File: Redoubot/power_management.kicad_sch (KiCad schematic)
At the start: 22 parts, among them U4 BQ25896RTWR, U5 BQ27220YZFR

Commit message: feat: added all remaining connectors & finished putting values on components
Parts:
- removed R19: 10m, Package_SON:Texas_S-PDSO-N12, symbol Device:R
- added C4: 1µF, symbol Device:C_Small
- added C5: 2.2µF, symbol Device:C_Small
- added C6: 470nF, symbol Device:C_Small
- added R2: 10k, Package_DFN_QFN:QFN-56-1EP_7x7mm_P0.4mm_EP5.6x5.6mm, symbol Device:R_Small_US
- added R3: 10m, Resistor_THT:R_Array_SIP4, symbol Device:R_Small_US
- added R4: 10k, symbol Device:R_Small_US
- R15, R16: value R -> 2.2k
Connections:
- net BAT: now also U5.C1 (SRP), U5.C3 (BAT), C4.1, R3.2
- net GND: now also U5.B2 (VSS), C4.2, C5.2, C6.2, R4.1
- net SCL_BAT: now also U5.A3 (SCL)
- net SDA_BAT: now also U5.A2 (SDA)
- net BAT_CHG: now reaches C15.2, C17.2, U4.13 (BAT), U4.14 (BAT)
- net BAT_CHG: now also U5.C2 (SRN), R3.1
- net GPOUT_FUEL_GAUGE: now reaches U5.A1 (GPOUT)
- net GPOUT_FUEL_GAUGE: now also R2.2
- net at U5.B1 (VIN): now also R4.2
- net at U5.B3 (VDD): now also C5.1, C6.1
- new net +3.3V: R2.1
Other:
- note added: "Fuel Gauge"
- moved on the sheet: U5

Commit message: chore: wired everything possible atm, wrote down every missing links, waiting for .ioc to continue
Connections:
- net 3.3V is gone; now on net +3.3V: R11.1, R13.1, R14.1
- net 5V renamed +5V
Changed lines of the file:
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@@
 	(wire
 		(pts
-			(xy 152.4 63.5) (xy 165.1 63.5)
+			(xy 157.48 63.5) (xy 165.1 63.5)
 		)
 		(stroke
@@
 	(wire
 		(pts
-			(xy 162.56 43.18) (xy 161.29 43.18)
+			(xy 162.56 43.18) (xy 157.48 43.18)
 		)
 		(stroke
@@
 	(wire
 		(pts
-			(xy 152.4 60.96) (xy 165.1 60.96)
+			(xy 157.48 60.96) (xy 165.1 60.96)
 		)
 		(stroke
@@
 	(wire
 		(pts
-			(xy 222.25 71.12) (xy 227.33 71.12)
+			(xy 222.25 71.12) (xy 240.03 71.12)
 		)
 		(stroke
@@
 	(wire
 		(pts
-			(xy 152.4 55.88) (xy 162.56 55.88)
+			(xy 157.48 55.88) (xy 162.56 55.88)
 		)
 		(stroke
@@
 			)
 			(justify right bottom)
-		)
-	)
-	(global_label "+3.3V"
-		(shape input)
-		(at 161.29 43.18 180)
-		(fields_autoplaced yes)
-		(effects
-			(font
-				(size 1.27 1.27)
-			)
-			(justify right)
-		)
-		(property "Intersheetrefs" "${INTERSHEET_REFS}"
-			(at 152.62 43.18 0)
-			(hide yes)
-			(show_name no)
-			(do_not_autoplace no)
-			(effects
-				(font
-					(size 1.27 1.27)
-				)
-				(justify right)
-			)
 		)
 	)
@@
 	(hierarchical_label "GPOUT_FUEL_GAUGE"
 		(shape output)
-		(at 152.4 55.88 180)
+		(at 157.48 55.88 180)
 		(effects
 			(font
@@
 		)
 	)
-	(hierarchical_label "5V"
+	(hierarchical_label "+5V"
 		(shape input)
 		(at 52.07 27.94 0)
@@
 		)
 	)
+	(hierarchical_label "+3.3V"
+		(shape input)
+		(at 157.48 43.18 180)
+		(effects
+			(font
+				(size 1.27 1.27)
+			)
+			(justify right)
+		)
+	)
 	(hierarchical_label "BAT"
 		(shape input)
-		(at 227.33 71.12 0)
+		(at 240.03 71.12 0)
 		(effects
 			(font
@@
 	(hierarchical_label "SDA_BAT"
 		(shape bidirectional)
-		(at 152.4 60.96 180)
+		(at 157.48 60.96 180)
 		(effects
 			(font
@@
 		)
 	)
-	(hierarchical_label "3.3V"
+	(hierarchical_label "+3.3V"
 		(shape input)
 		(at 31.75 102.87 180)
@@
 	(hierarchical_label "SCL_BAT"
 		(shape input)
-		(at 152.4 63.5 180)
-		(effects
-			(font
+		(at 157.48 63.5 180)
+		(effects
+			(font

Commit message: simply added the JLCPCB Part # as an LCSC field in the component descriptions
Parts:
- U4: footprint RTW0024H -> footprints_BQ25:RTW0024H; LCSC (none) -> C181475
- U5: footprint YZF9_TEX -> footprints_BQ27:YZF9_TEX; LCSC (none) -> C528617
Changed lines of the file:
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@@
 			)
 		)
-		(property "Footprint" "RTW0024H"
+		(property "Footprint" "footprints_BQ25:RTW0024H"
 			(at 78.74 62.23 0)
 			(hide yes)
@@
 		)
 		(property "Description" ""
+			(at 78.74 62.23 0)
+			(hide yes)
+			(show_name no)
+			(do_not_autoplace no)
+			(effects
+				(font
+					(size 1.27 1.27)
+				)
+			)
+		)
+		(property "LCSC" "C181475"
 			(at 78.74 62.23 0)
 			(hide yes)
@@
 			)
 		)
-		(property "Footprint" "YZF9_TEX"
+		(property "Footprint" "footprints_BQ27:YZF9_TEX"
 			(at 165.1 58.42 0)
 			(hide yes)
@@
 			(at 165.1 58.42 0)
 			(hide yes)
+			(show_name no)
+			(do_not_autoplace no)
+			(effects
+				(font
+					(size 1.27 1.27)
+				)
+			)
+		)
+		(property "LCSC" "C528617"
+			(at 165.1 58.42 0)
+			(hide yes)

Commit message: Added footprints for capacitors
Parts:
- C11, C13, C14: footprint (none) -> Capacitor_SMD:C_0603_1608Metric
- C12, C15, C16, C17, C18: footprint (none) -> Capacitor_SMD:C_0805_2012Metric
- C4, C5, C6: footprint (none) -> Capacitor_SMD:C_0402_1005Metric
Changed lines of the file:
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@@
 			)
 		)
-		(property "Footprint" ""
+		(property "Footprint" "Capacitor_SMD:C_0805_2012Metric"
 			(at 58.42 38.4048 0)
 			(hide yes)
@@
 			)
 		)
-		(property "Footprint" ""
+		(property "Footprint" "Capacitor_SMD:C_0805_2012Metric"
 			(at 132.3848 31.75 0)
 			(hide yes)
@@
 			)
 		)
-		(property "Footprint" ""
+		(property "Footprint" "Capacitor_SMD:C_0402_1005Metric"
 			(at 234.95 59.69 0)
 			(hide yes)
@@
 			)
 		)
-		(property "Footprint" ""
+		(property "Footprint" "Capacitor_SMD:C_0805_2012Metric"
 			(at 123.4948 66.04 0)
 			(hide yes)
@@
 			)
 		)
-		(property "Footprint" ""
+		(property "Footprint" "Capacitor_SMD:C_0402_1005Metric"
 			(at 154.94 76.2 0)
 			(hide yes)
@@
 			)
 		)
-		(property "Footprint" ""
+		(property "Footprint" "Capacitor_SMD:C_0603_1608Metric"
 			(at 41.91 30.7848 0)
 			(hide yes)
@@
 			)
 		)
-		(property "Footprint" ""
+		(property "Footprint" "Capacitor_SMD:C_0603_1608Metric"
 			(at 101.9048 31.75 0)
 			(hide yes)
@@
 			)
 		)
-		(property "Footprint" ""
+		(property "Footprint" "Capacitor_SMD:C_0402_1005Metric"
 			(at 162.56 76.2 0)
 			(hide yes)
@@
 			)
 		)
-		(property "Footprint" ""
+		(property "Footprint" "Capacitor_SMD:C_0805_2012Metric"
 			(at 113.3348 66.04 0)
 			(hide yes)
@@
 			)
 		)
-		(property "Footprint" ""
+		(property "Footprint" "Capacitor_SMD:C_0603_1608Metric"
 			(at 108.2548 44.45 0)
 			(hide yes)
@@
 			)
 		)
-		(property "Footprint" ""
+		(property "Footprint" "Capacitor_SMD:C_0805_2012Metric"
 			(at 122.2248 31.75 0)
 			(hide yes)

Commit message: Added the footprints for the resistors, inductors and the crystal
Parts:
- D3, D4: footprint (none) -> LED_SMD:LED_0603_1608Metric
- L2: footprint (none) -> Inductor_SMD:L_Coilcraft_XxL4020
- R11, R12, R13, R14, R15, R16, R17, R18, R4: footprint (none) -> Resistor_SMD:R_0603_1608Metric
- R2: footprint Package_DFN_QFN:QFN-56-1EP_7x7mm_P0.4mm_EP5.6x5.6mm -> Resistor_SMD:R_0603_1608Metric
- R3: footprint Resistor_THT:R_Array_SIP4 -> Resistor_SMD:R_0805_2012Metric
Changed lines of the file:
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@@
 			)
 		)
-		(property "Footprint" ""
+		(property "Footprint" "LED_SMD:LED_0603_1608Metric"
 			(at 46.99 59.69 0)
 			(hide yes)
@@
 			)
 		)
-		(property "Footprint" ""
+		(property "Footprint" "LED_SMD:LED_0603_1608Metric"
 			(at 46.99 66.04 0)
 			(hide yes)
@@
 			)
 		)
-		(property "Footprint" ""
+		(property "Footprint" "Resistor_SMD:R_0603_1608Metric"
 			(at 54.61 67.818 90)
 			(hide yes)
@@
 			)
 		)
-		(property "Footprint" ""
+		(property "Footprint" "Resistor_SMD:R_0603_1608Metric"
 			(at 39.878 87.63 90)
 			(hide yes)
@@
 			)
 		)
-		(property "Footprint" ""
+		(property "Footprint" "Resistor_SMD:R_0603_1608Metric"
 			(at 210.82 59.69 0)
 			(hide yes)
@@
 			)
 		)
-		(property "Footprint" "Package_DFN_QFN:QFN-56-1EP_7x7mm_P0.4mm_EP5.6x5.6mm"
+		(property "Footprint" "Resistor_SMD:R_0603_1608Metric"
 			(at 162.56 50.8 0)
 			(hide yes)
@@
 			)
 		)
-		(property "Footprint" ""
+		(property "Footprint" "Resistor_SMD:R_0603_1608Metric"
 			(at 46.228 87.63 90)
 			(hide yes)
@@
 			)
 		)
-		(property "Footprint" ""
+		(property "Footprint" "Inductor_SMD:L_Coilcraft_XxL4020"
 			(at 113.03 31.75 0)
 			(hide yes)
@@
 			)
 		)
-		(property "Footprint" "Resistor_THT:R_Array_SIP4"
+		(property "Footprint" "Resistor_SMD:R_0805_2012Metric"
 			(at 219.71 71.12 0)
 			(hide yes)
@@
 			)
 		)
-		(property "Footprint" ""
+		(property "Footprint" "Resistor_SMD:R_0603_1608Metric"
 			(at 36.83 53.848 90)
 			(hide yes)
@@
 			)
 		)
-		(property "Footprint" ""
+		(property "Footprint" "Resistor_SMD:R_0603_1608Metric"
 			(at 107.188 82.55 90)
 			(hide yes)
@@
 			)
 		)
-		(property "Footprint" ""
+		(property "Footprint" "Resistor_SMD:R_0603_1608Metric"
 			(at 107.188 91.44 90)
 			(hide yes)
@@
 			)
 		)
-		(property "Footprint" ""
+		(property "Footprint" "Resistor_SMD:R_0603_1608Metric"
 			(at 33.528 87.63 90)
 			(hide yes)
@@
 			)
 		)
-		(property "Footprint" ""
+		(property "Footprint" "Resistor_SMD:R_0603_1608Metric"
 			(at 54.61 61.468 90)
 			(hide yes)

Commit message: feat: added usb_c charging + flashing, added +3.3V generation, added HM10 & DFMini Support, wired everything and modified ioc accordingly
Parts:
- added R19: 10k, symbol Device:R_Small_US
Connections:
- net GND: now also R19.2
- net OTG_EN: now reaches U4.8 (OTG_IUSB)
- net OTG_EN: now also R19.1
- no-connect marks 3 -> 2
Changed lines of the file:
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@@
 	)
 	(junction
-		(at 50.8 82.55)
+		(at 48.26 82.55)
+		(diameter 0)
+		(color 0 0 0 0)
+	)
+	(junction
+		(at 55.88 92.71)
 		(diameter 0)
 		(color 0 0 0 0)
@@
 	)
 	(junction
+		(at 55.88 87.63)
+		(diameter 0)
+		(color 0 0 0 0)
+	)
+	(junction
 		(at 123.19 31.75)
 		(diameter 0)
@@
 	)
 	(no_connect
-		(at 58.42 87.63)
-	)
-	(no_connect
 		(at 58.42 96.52)
 	)
@@
 	(wire
 		(pts
-			(xy 58.42 92.71) (xy 53.34 92.71)
+			(xy 58.42 92.71) (xy 55.88 92.71)
 		)
 		(stroke
@@
 	(wire
 		(pts
-			(xy 50.8 82.55) (xy 44.45 82.55)
+			(xy 44.45 82.55) (xy 58.42 82.55)
 		)
 		(stroke
@@
 	(wire
 		(pts
+			(xy 55.88 87.63) (xy 58.42 87.63)
+		)
+		(stroke
+			(width 0)
+			(type default)
+		)
+	)
+	(wire
+		(pts
 			(xy 99.06 59.69) (xy 99.06 62.23)
 		)
@@
 	(wire
 		(pts
+			(xy 48.26 80.01) (xy 48.26 82.55)
+		)
+		(stroke
+			(width 0)
+			(type default)
+		)
+	)
+	(wire
+		(pts
 			(xy 99.06 50.8) (xy 109.22 50.8)
 		)
@@
 	(wire
 		(pts
-			(xy 53.34 92.71) (xy 53.34 96.52)
+			(xy 55.88 92.71) (xy 55.88 99.06)
 		)
 		(stroke
@@
 	(wire
 		(pts
-			(xy 99.06 31.75) (xy 99.06 34.29)
-		)
-		(stroke
-			(width 0)
-			(type default)
-		)
-	)
-	(wire
-		(pts
-			(xy 207.01 58.42) (xy 205.74 58.42)
+			(xy 55.88 86.36) (xy 55.88 87.63)
 		)
 		(stroke
@@
 	(wire
 		(pts
-			(xy 102.87 31.75) (xy 109.22 31.75)
+			(xy 99.06 31.75) (xy 99.06 34.29)
 		)
 		(stroke
@@
 	(wire
 		(pts
-			(xy 31.75 52.07) (xy 31.75 46.99)
+			(xy 207.01 58.42) (xy 205.74 58.42)
 		)
 		(stroke
@@
 	(wire
 		(pts
-			(xy 50.8 82.55) (xy 50.8 87.63)
+			(xy 102.87 31.75) (xy 109.22 31.75)
 		)
 		(stroke
@@
 	(wire
 		(pts
-			(xy 50.8 82.55) (xy 58.42 82.55)
+			(xy 31.75 52.07) (xy 31.75 46.99)
 		)
 		(stroke
@@
 	)
 	(hierarchical_label "SYS"
-		(shape input)
+		(shape output)
 		(at 43.18 66.04 180)
 		(effects
@@
 	)
 	(hierarchical_label "+5V"
-		(shape input)
+		(shape bidirectional)
 		(at 52.07 27.94 0)
 		(effects
@@
 	)
 	(hierarchical_label "SYS"
-		(shape input)
+		(shape output)
 		(at 137.16 31.75 0)
 		(effects
@@
 	(hierarchical_label "PWR_INT"
 		(shape input)
-		(at 50.8 87.63 270)
+		(at 48.26 80.01 180)
 		(effects
 			(font
@@
 		)
 	)
+	(hierarchical_label "OTG_EN"
+		(shape input)
+		(at 55.88 86.36 180)
+		(effects
+			(font
+				(size 1.27 1.27)
+			)
+			(justify right)
+		)
+	)
 	(hierarchical_label "SDA_BAT"
 		(shape bidirectional)
@@
 	)
 	(hierarchical_label "SYS"
-		(shape input)
+		(shape output)
 		(at 43.18 59.69 180)
 		(effects
@@
 	(symbol
 		(lib_id "power:GND")
-		(at 53.34 96.52 0)
+		(at 55.88 99.06 0)
 		(unit 1)
 		(body_style 1)
@@
 		(fields_autoplaced yes)
 		(property "Reference" "#PWR015"
-			(at 53.34 102.87 0)
+			(at 55.88 105.41 0)
 			(hide yes)
 			(show_name no)
@@
 		)
 		(property "Value" "GND"
-			(at 53.34 101.6 0)
+			(at 55.88 104.14 0)
 			(show_name no)
 			(do_not_autoplace no)
@@
 		)
 		(property "Footprint" ""
-			(at 53.34 96.52 0)
+			(at 55.88 99.06 0)
 			(hide yes)
 			(show_name no)
@@
 		)
 		(property "Datasheet" ""
-			(at 53.34 96.52 0)
+			(at 55.88 99.06 0)
 			(hide yes)
 			(show_name no)
@@
 		)
 		(property "Description" "Power symbol creates a global label with name \"GND\" , ground"
-			(at 53.34 96.52 0)
+			(at 55.88 99.06 0)
 			(hide yes)
 			(show_name no)
@@
 					(unit 1)
 				)
+			)
+		)
+	)
+	(symbol
+		(lib_id "Device:R_Small_US")
+		(at 55.88 90.17 0)
+		(unit 1)
+		(body_style 1)
+		(exclude_from_sim no)
+		(in_bom yes)
+		(on_board yes)
+		(in_pos_files yes)
+		(dnp no)
+		(property "Reference" "R19"
+			(at 57.15 88.9 0)
+			(show_name no)
+			(do_not_autoplace no)
+			(effects
+				(font
+					(size 1.27 1.27)
+				)
+				(justify left)
+			)
+		)
+		(property "Value" "10k"
+			(at 57.15 90.678 0)
+			(show_name no)
+			(do_not_autoplace no)
+			(effects
+				(font
+					(size 1.27 1.27)
+				)
+				(justify left)
+			)
+		)
+		(property "Footprint" ""
+			(at 55.88 90.17 0)
+			(hide yes)
+			(show_name no)
+			(do_not_autoplace no)
+			(effects
+				(font
+					(size 1.27 1.27)
+				)
+			)
+		)
+		(property "Datasheet" ""
+			(at 55.88 90.17 0)
+			(hide yes)
+			(show_name no)
+			(do_not_autoplace no)
+			(effects
+				(font
+					(size 1.27 1.27)
+				)
+			)
+		)
+		(property "Description" "Resistor, small US symbol"
+			(at 55.88 90.17 0)
+			(hide yes)
+			(show_name no)
+			(do_not_autoplace no)
+			(effects
+				(font
+					(size 1.27 1.27)
+				)
+			)
+		)
+		(pin "1"
+		)
+		(pin "2"
+		)
+		(instances
+			(project "Redoubot"
+				(path "/43131b41-4104-4cd6-9c2f-4d5da1687300/73350c17-84ab-42d8-b086-6cfec23927e8"
+					(reference "R19")
+					(unit 1)
+				)

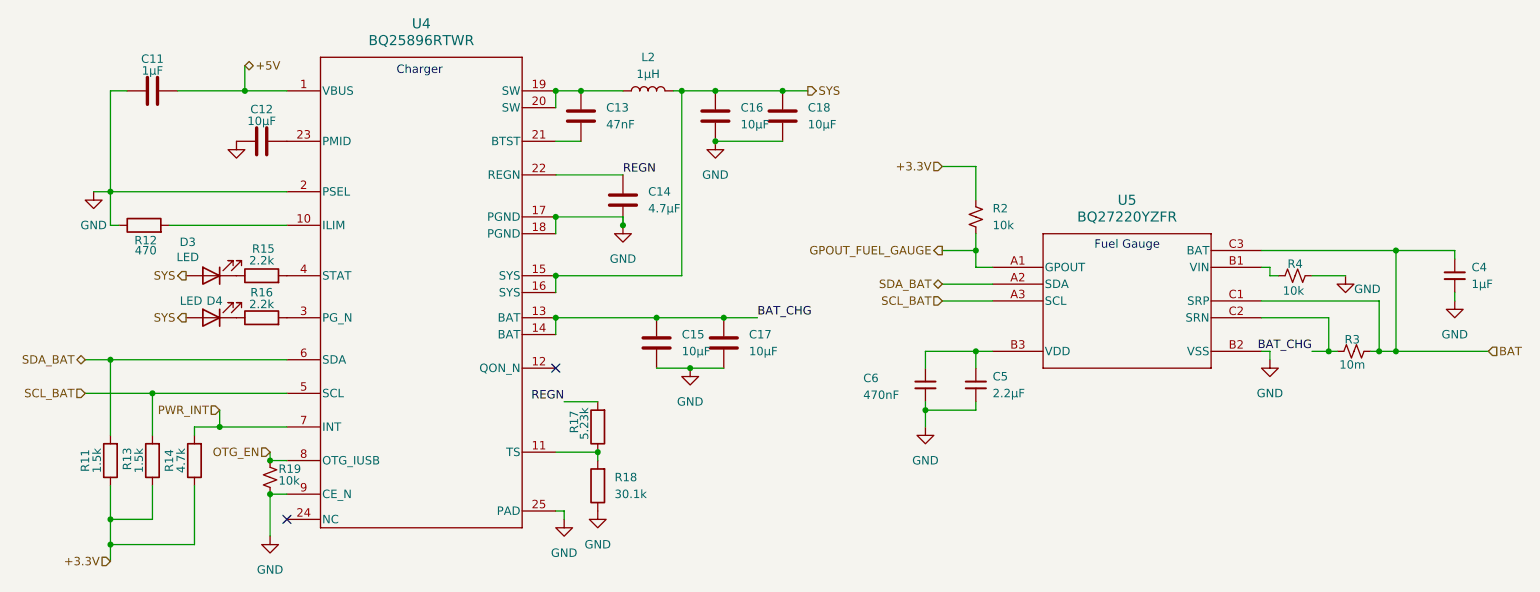
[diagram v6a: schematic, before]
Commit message: chore: added jumpers, changed 5v stm input to 3v3
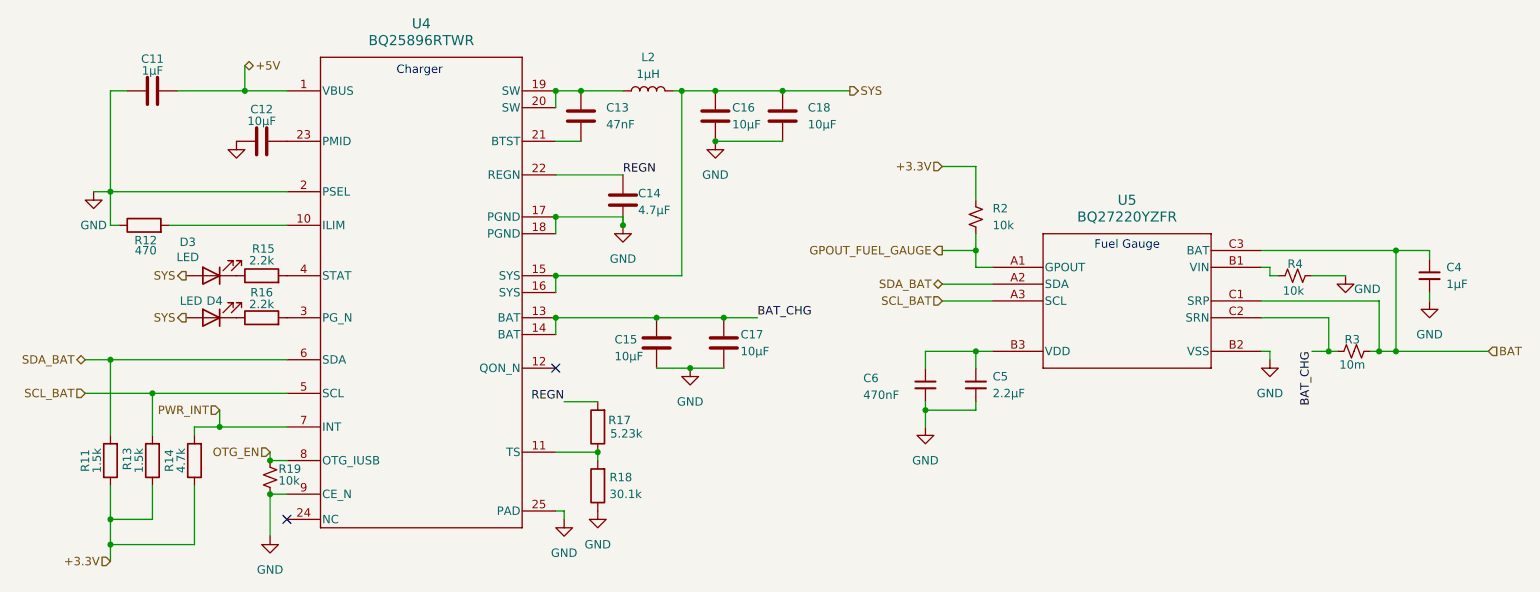
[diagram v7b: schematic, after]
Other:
- moved on the sheet: C4
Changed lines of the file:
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@@
 	)
 	(junction
-		(at 123.19 39.37)
-		(diameter 0)
-		(color 0 0 0 0)
-	)
-	(junction
 		(at 162.56 71.12)
 		(diameter 0)
@@
 	)
 	(junction
+		(at 123.19 39.37)
+		(diameter 0)
+		(color 0 0 0 0)
+	)
+	(junction
 		(at 105.41 86.36)
 		(diameter 0)
@@
 	(wire
 		(pts
-			(xy 133.35 31.75) (xy 137.16 31.75)
+			(xy 133.35 31.75) (xy 143.51 31.75)
 		)
 		(stroke
@@
 	(wire
 		(pts
-			(xy 123.19 39.37) (xy 133.35 39.37)
-		)
-		(stroke
-			(width 0)
-			(type default)
-		)
-	)
-	(wire
-		(pts
 			(xy 44.45 82.55) (xy 58.42 82.55)
 		)
@@
 	(wire
 		(pts
-			(xy 205.74 55.88) (xy 234.95 55.88)
+			(xy 205.74 55.88) (xy 231.14 55.88)
 		)
 		(stroke
@@
 	(wire
 		(pts
+			(xy 123.19 39.37) (xy 133.35 39.37)
+		)
+		(stroke
+			(width 0)
+			(type default)
+		)
+	)
+	(wire
+		(pts
 			(xy 27.94 72.39) (xy 31.75 72.39)
 		)
@@
 	(wire
 		(pts
-			(xy 234.95 63.5) (xy 234.95 62.23)
+			(xy 231.14 63.5) (xy 231.14 62.23)
 		)
 		(stroke
@@
 	(wire
 		(pts
-			(xy 234.95 55.88) (xy 234.95 57.15)
+			(xy 231.14 55.88) (xy 231.14 57.15)
 		)
 		(stroke
@@
 	)
 	(label "BAT_CHG"
-		(at 213.36 71.12 180)
+		(at 213.36 71.12 270)
 		(effects
 			(font
@@
 	(hierarchical_label "SYS"
 		(shape output)
-		(at 137.16 31.75 0)
+		(at 143.51 31.75 0)
 		(effects
 			(font
@@
 	(symbol
 		(lib_id "Device:C_Small")
-		(at 234.95 59.69 0)
+		(at 231.14 59.69 0)
 		(unit 1)
 		(body_style 1)
@@
 		(fields_autoplaced yes)
 		(property "Reference" "C4"
-			(at 237.49 58.4199 0)
+			(at 233.68 58.4199 0)
 			(show_name no)
 			(do_not_autoplace no)
@@
 		)
 		(property "Value" "1µF"
-			(at 237.49 60.9599 0)
+			(at 233.68 60.9599 0)
 			(show_name no)
 			(do_not_autoplace no)
@@
 		)
 		(property "Footprint" "Capacitor_SMD:C_0402_1005Metric"
-			(at 234.95 59.69 0)
+			(at 231.14 59.69 0)
 			(hide yes)
 			(show_name no)
@@
 		)
 		(property "Datasheet" ""
-			(at 234.95 59.69 0)
+			(at 231.14 59.69 0)
 			(hide yes)
 			(show_name no)
@@
 		)
 		(property "Description" "Unpolarized capacitor, small symbol"
-			(at 234.95 69.85 0)
+			(at 231.14 69.85 0)
 			(hide yes)
 			(show_name no)
@@
 		(in_pos_files yes)
 		(dnp no)
-		(fields_autoplaced yes)
 		(property "Reference" "C17"
-			(at 128.27 68.5799 0)
+			(at 127 68.58 0)
 			(show_name no)
 			(do_not_autoplace no)
@@
 		)
 		(property "Value" "10µF"
-			(at 128.27 71.1199 0)
+			(at 127 71.12 0)
 			(show_name no)
 			(do_not_autoplace no)
@@
 	(symbol
 		(lib_id "power:GND")
-		(at 234.95 63.5 0)
+		(at 231.14 63.5 0)
 		(unit 1)
 		(body_style 1)
@@
 		(fields_autoplaced yes)
 		(property "Reference" "#PWR06"
-			(at 234.95 69.85 0)
+			(at 231.14 69.85 0)
 			(hide yes)
 			(show_name no)
@@
 		)
 		(property "Value" "GND"
-			(at 234.95 68.58 0)
+			(at 231.14 68.58 0)
 			(show_name no)
 			(do_not_autoplace no)
@@
 		)
 		(property "Footprint" ""
-			(at 234.95 63.5 0)
+			(at 231.14 63.5 0)
 			(hide yes)
 			(show_name no)
@@
 		)
 		(property "Datasheet" ""
-			(at 234.95 63.5 0)
+			(at 231.14 63.5 0)
 			(hide yes)
 			(show_name no)
@@
 		)
 		(property "Description" "Power symbol creates a global label with name \"GND\" , ground"
-			(at 234.95 63.5 0)
+			(at 231.14 63.5 0)
 			(hide yes)
 			(show_name no)
@@
 		(in_pos_files yes)
 		(dnp no)
-		(fields_autoplaced yes)
 		(property "Reference" "C15"
-			(at 118.11 68.5799 0)
+			(at 107.95 69.342 0)
 			(show_name no)
 			(do_not_autoplace no)
@@
 		)
 		(property "Value" "10µF"
-			(at 118.11 71.1199 0)
+			(at 107.95 71.882 0)
 			(show_name no)
 			(do_not_autoplace no)
@@
 		(dnp no)
 		(property "Reference" "R17"
-			(at 101.854 81.788 90)
+			(at 108.712 81.534 0)
 			(show_name no)
 			(do_not_autoplace no)
@@
 		)
 		(property "Value" "5.23k"
-			(at 103.378 82.042 90)
+			(at 109.728 83.566 0)
 			(show_name no)
 			(do_not_autoplace no)
@@
 		(in_pos_files yes)
 		(dnp no)
-		(fields_autoplaced yes)
 		(property "Reference" "C14"
-			(at 113.03 46.9899 0)
+			(at 111.506 47.244 0)
 			(show_name no)
 			(do_not_autoplace no)
@@
 		)
 		(property "Value" "4.7µF"
-			(at 113.03 49.5299 0)
+			(at 111.506 49.784 0)
 			(show_name no)
 			(do_not_autoplace no)
@@
 		(in_pos_files yes)
 		(dnp no)
-		(fields_autoplaced yes)
 		(property "Reference" "R18"
-			(at 107.95 90.1699 0)
+			(at 107.188 90.17 0)
 			(show_name no)
 			(do_not_autoplace no)
@@
 		)
 		(property "Value" "30.1k"
-			(at 107.95 92.7099 0)
+			(at 107.188 92.71 0)
 			(show_name no)
 			(do_not_autoplace no)
@@
 		(in_pos_files yes)
 		(dnp no)
-		(fields_autoplaced yes)
 		(property "Reference" "C16"
-			(at 127 34.2899 0)
+			(at 125.73 34.2899 0)
 			(show_name no)
 			(do_not_autoplace no)
@@
 		)
 		(property "Value" "10µF"
-			(at 127 36.8299 0)
+			(at 125.73 36.8299 0)
 			(show_name no)
 			(do_not_autoplace no)
